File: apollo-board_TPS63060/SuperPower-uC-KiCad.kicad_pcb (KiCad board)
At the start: 4 copper layers, 45.1 x 45.1 mm, 114 parts, among them J1 JST_PH_S2B_thru, J10 Conn_01x13_Male, J11 Conn_01x04_Male, J3 Conn_01x02_Male, J4 DNP/JST_ZH_S2B_thru, J5 DNP/JST_XH_S2B_thru, J6 Conn_01x02_Male, Q1 DMN2019UTS, Q10 2N7002A, Q11 2N7002A, Q12 DMP2035UVT, Q13 DMP2035UVT, Q14 DMP2035UVT, Q15 DMN3023L, Q2 Si3421DV, Q3 DMN3023L, Q4 2N7002A, Q5 DMP2035UVT, Q6 BSS84-7-F, Q9 2N7002A, SW1 DNP/SKRKAEE020, U1 AP9101CK6-AYTRG1, U10 TPS63060, U2 USB-C, U3 IP4220CZ6, U4 LTC4162EUFD-LAD, U5 RV-3028-C7, U6 TPS70933DBV, U9 TPS63060

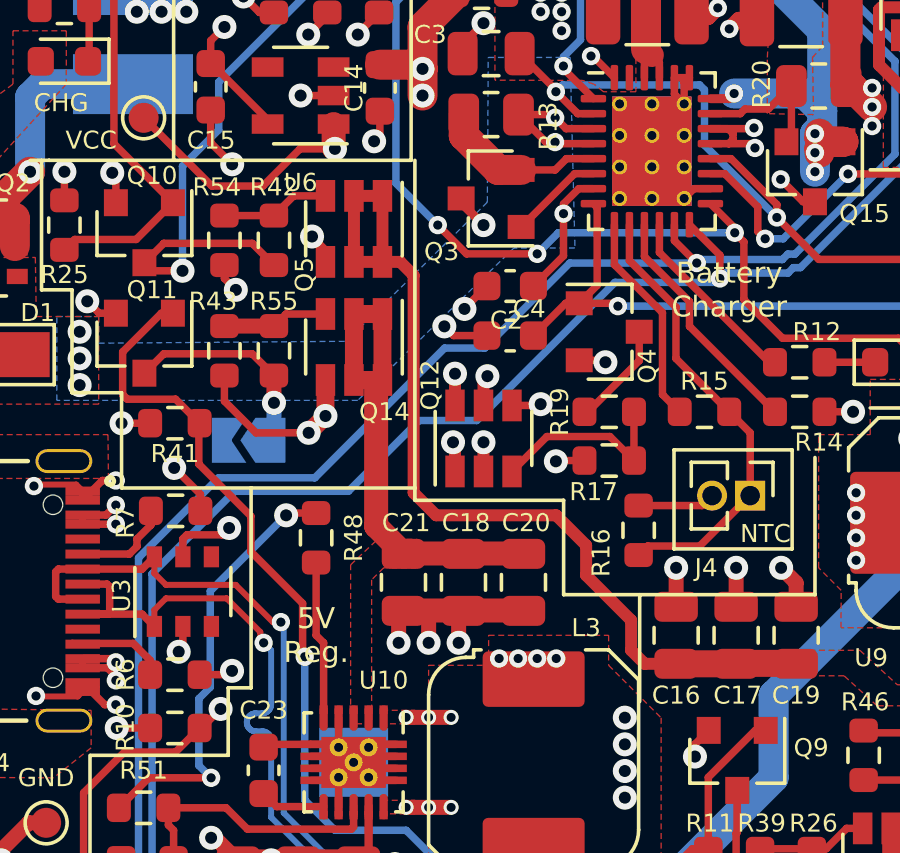
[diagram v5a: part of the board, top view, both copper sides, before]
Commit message: Improve Power Tracks width and Vias on Top Layer (+3.3V)
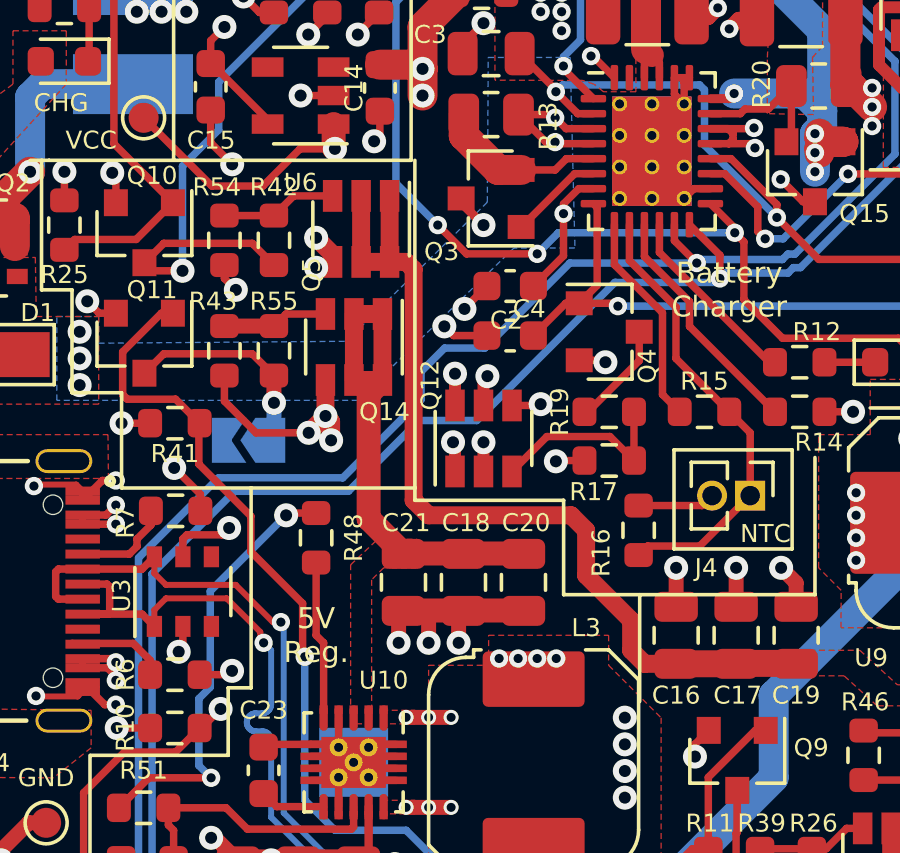
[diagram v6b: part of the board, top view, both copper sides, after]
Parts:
- moved Q5 0.24 mm to (133.6, 93.2)
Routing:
- net VCC: track 26.2 -> 27.7 mm, vias 11 -> 13
- net /Regulator and Cut-Off Module/3v3_Reg_Vin: track 31.1 -> 30.4 mm
- net /SCL: track 73.0 -> 73.6 mm
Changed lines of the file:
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@@
     (thickness 1.6)
     (drawings 122)
-    (tracks 1001)
+    (tracks 1009)
     (zones 0)
     (modules 114)
@@
   (layers
     (0 F.Cu signal)
-    (1 In1.Cu power hide)
-    (2 In2.Cu signal hide)
+    (1 In1.Cu power)
+    (2 In2.Cu signal)
     (31 B.Cu signal)
     (32 B.Adhes user)
@@
     (34 B.Paste user)
     (35 F.Paste user)
-    (36 B.SilkS user)
-    (37 F.SilkS user)
+    (36 B.SilkS user hide)
+    (37 F.SilkS user hide)
     (38 B.Mask user)
     (39 F.Mask user)
@@
   )
   (setup
-    (last_trace_width 0.25)
+    (last_trace_width 0.6)
     (user_trace_width 0.2)
     (user_trace_width 0.25)
@@
   )
   (module Package_TO_SOT_SMD:SOT-23-6 (layer F.Cu)
-    (at 133.35 93.218 270)
+    (at 133.589 93.218 270)
     (descr "6-pin SOT-23 package")
     (tags SOT-23-6)
@@
   (gr_line (start 160.5534 75.1332) (end 120.4722 75.1332) (layer Edge.Cuts) (width 0.05))
   (gr_line (start 120.523 120.2436) (end 160.5026 120.2436) (layer Edge.Cuts) (width 0.05))
+  (via (at 132.089 94.515) (size 0.8) (drill 0.4) (layers F.Cu B.Cu) (net 9))
   (via (at 153.035 80.9625) (size 0.8) (drill 0.4) (layers F.Cu B.Cu) (net 1))
   (segment (start 152.7885 81.209) (end 153.035 80.9625) (width 0.4) (layer F.Cu) (net 1))
@@
   (via (at 136.652 100.33) (size 0.8) (drill 0.4) (layers F.Cu B.Cu) (net 9))
   (via (at 137.668 100.33) (size 0.8) (drill 0.4) (layers F.Cu B.Cu) (net 9))
-  (via (at 131.953 93.472) (size 0.8) (drill 0.4) (layers F.Cu B.Cu) (net 9))
-  (segment (start 132.4 93.919) (end 131.953 93.472) (width 0.25) (layer F.Cu) (net 9))
-  (segment (start 132.4 94.318) (end 132.4 93.919) (width 0.25) (layer F.Cu) (net 9))
+  (via (at 132.089 93.515) (size 0.8) (drill 0.4) (layers F.Cu B.Cu) (net 9))
   (via (at 129.413 95.25) (size 0.8) (drill 0.4) (layers F.Cu B.Cu) (net 9))
   (segment (start 129.032 94.869) (end 129.413 95.25) (width 0.25) (layer F.Cu) (net 9))
@@
   (segment (start 129.032 98.107) (end 129.032 98.958) (width 0.25) (layer F.Cu) (net 9))
   (segment (start 129.032 98.958) (end 130.089 100.015) (width 0.25) (layer F.Cu) (net 9))
+  (segment (start 132.639 94.065) (end 132.089 93.515) (width 0.6) (layer F.Cu) (net 9))
+  (segment (start 132.639 94.318) (end 132.639 94.065) (width 0.6) (layer F.Cu) (net 9))
+  (segment (start 132.442 94.515) (end 132.639 94.318) (width 0.6) (layer F.Cu) (net 9))
+  (segment (start 132.089 94.515) (end 132.442 94.515) (width 0.6) (layer F.Cu) (net 9))
+  (via (at 132.589 100.265) (size 0.8) (drill 0.4) (layers F.Cu B.Cu) (net 9))
+  (segment (start 132.589 99.643) (end 132.4 99.454) (width 0.6) (layer F.Cu) (net 9))
+  (segment (start 132.589 100.265) (end 132.589 99.643) (width 0.6) (layer F.Cu) (net 9))
   (segment (start 127.6477 104.1484) (end 127.6477 103.5484) (width 0.25) (layer F.Cu) (net 12))
   (segment (start 128.960468 103.41601) (end 129.188978 103.1875) (width 0.25) (layer F.Cu) (net 12))
@@
   (segment (start 140.543888 94.355477) (end 144.776433 94.355477) (width 0.25) (layer B.Cu) (net 14))
   (segment (start 137.707368 97.191997) (end 140.543888 94.355477) (width 0.25) (layer B.Cu) (net 14))
-  (segment (start 132.047001 101.515) (end 136.370004 97.191997) (width 0.25) (layer B.Cu) (net 14))
-  (segment (start 128.839 101.515) (end 132.047001 101.515) (width 0.25) (layer B.Cu) (net 14))
-  (segment (start 126.168989 104.185011) (end 128.839 101.515) (width 0.25) (layer B.Cu) (net 14))
   (segment (start 136.370004 97.191997) (end 137.707368 97.191997) (width 0.25) (layer B.Cu) (net 14))
+  (segment (start 135.589 98.903364) (end 135.589 97.973001) (width 0.25) (layer B.Cu) (net 14))
+  (segment (start 132.977364 101.515) (end 135.589 98.903364) (width 0.25) (layer B.Cu) (net 14))
+  (segment (start 135.589 97.973001) (end 136.370004 97.191997) (width 0.25) (layer B.Cu) (net 14))
+  (segment (start 128.839 101.515) (end 132.977364 101.515) (width 0.25) (layer B.Cu) (net 14))
+  (segment (start 126.168989 104.185011) (end 128.839 101.515) (width 0.25) (layer B.Cu) (net 14))
+  (segment (start 125.089 118.739) (end 125.089 115.39) (width 0.25) (layer B.Cu) (net 14))
   (segment (start 126.168989 114.310011) (end 126.168989 104.185011) (width 0.25) (layer B.Cu) (net 14))
   (segment (start 125.089 115.39) (end 126.168989 114.310011) (width 0.25) (layer B.Cu) (net 14))
-  (segment (start 125.089 118.739) (end 125.089 115.39) (width 0.25) (layer B.Cu) (net 14))
   (segment (start 125.222 118.872) (end 125.089 118.739) (width 0.25) (layer B.Cu) (net 14))
   (segment (start 130.683 100.465) (end 130.564 100.584) (width 0.6) (layer B.Cu) (net 31))
@@
   (segment (start 158.089 89.515) (end 161.29 89.535) (width 0.5) (layer F.Cu) (net 63))
   (segment (start 158.339 89.515) (end 158.089 89.515) (width 0.5) (layer F.Cu) (net 63))
-  (segment (start 134.3 92.118) (end 133.35 92.118) (width 0.4) (layer F.Cu) (net 64))
-  (segment (start 134.3 94.318) (end 133.35 94.318) (width 0.4) (layer F.Cu) (net 64))
-  (segment (start 133.35 92.118) (end 133.35 94.318) (width 0.4) (layer F.Cu) (net 64))
-  (segment (start 134.3 94.318) (end 134.3 92.118) (width 0.4) (layer F.Cu) (net 64))
   (segment (start 146.074 107.715) (end 146.089 107.7) (width 0.5) (layer F.Cu) (net 64))
   (segment (start 144.089 107.715) (end 146.074 107.715) (width 0.9) (layer F.Cu) (net 64))
   (segment (start 146.089 107.7) (end 148.089 107.7) (width 0.9) (layer F.Cu) (net 64))
-  (segment (start 142.589 106.265) (end 142.589 107.265) (width 0.4) (layer F.Cu) (net 64))
-  (segment (start 140.089 102.765) (end 141.089 103.765) (width 0.4) (layer F.Cu) (net 64))
-  (segment (start 136.089 102.765) (end 140.089 102.765) (width 0.4) (layer F.Cu) (net 64))
-  (segment (start 141.089 103.765) (end 141.089 104.765) (width 0.4) (layer F.Cu) (net 64))
-  (segment (start 135.339 102.015) (end 136.089 102.765) (width 0.4) (layer F.Cu) (net 64))
-  (segment (start 141.089 104.765) (end 142.589 106.265) (width 0.4) (layer F.Cu) (net 64))
-  (segment (start 135.339 94.765) (end 135.339 102.015) (width 0.4) (layer F.Cu) (net 64))
-  (segment (start 143.039 107.715) (end 144.089 107.715) (width 0.4) (layer F.Cu) (net 64))
-  (segment (start 142.589 107.265) (end 143.039 107.715) (width 0.4) (layer F.Cu) (net 64))
-  (segment (start 134.892 94.318) (end 135.339 94.765) (width 0.4) (layer F.Cu) (net 64))
-  (segment (start 134.3 94.318) (end 134.892 94.318) (width 0.4) (layer F.Cu) (net 64))
+  (segment (start 133.589 92.118) (end 133.589 94.318) (width 0.6) (layer F.Cu) (net 64))
+  (segment (start 134.539 94.318) (end 133.589 94.318) (width 0.6) (layer F.Cu) (net 64))
+  (segment (start 134.539 92.118) (end 134.539 94.318) (width 0.6) (layer F.Cu) (net 64))
+  (segment (start 143.039 107.715) (end 144.089 107.715) (width 0.6) (layer F.Cu) (net 64))
+  (segment (start 142.589 107.265) (end 143.039 107.715) (width 0.6) (layer F.Cu) (net 64))
+  (segment (start 141.089 104.765) (end 142.589 106.265) (width 0.6) (layer F.Cu) (net 64))
+  (segment (start 141.089 103.265) (end 141.089 104.765) (width 0.6) (layer F.Cu) (net 64))
+  (segment (start 142.589 106.265) (end 142.589 107.265) (width 0.6) (layer F.Cu) (net 64))
+  (segment (start 135.839 102.765) (end 140.589 102.765) (width 0.6) (layer F.Cu) (net 64))
+  (segment (start 135.339 102.265) (end 135.839 102.765) (width 0.6) (layer F.Cu) (net 64))
+  (segment (start 135.339 94.568) (end 135.339 102.265) (width 0.6) (layer F.Cu) (net 64))
+  (segment (start 140.589 102.765) (end 141.089 103.265) (width 0.6) (layer F.Cu) (net 64))
+  (segment (start 135.089 94.318) (end 135.339 94.568) (width 0.6) (layer F.Cu) (net 64))
+  (segment (start 134.539 94.318) (end 135.089 94.318) (width 0.6) (layer F.Cu) (net 64))
   (segment (start 155.064 111.661) (end 154 112.725) (width 0.25) (layer F.Cu) (net 65))
   (segment (start 155.064 110.015) (end 155.064 111.661) (width 0.25) (layer F.Cu) (net 65))
@@
   (segment (start 134.3 96.055) (end 134.3 98.255) (width 0.6) (layer F.Cu) (net 67))
   (segment (start 134.089 98.466) (end 134.3 98.255) (width 0.6) (layer F.Cu) (net 67))
-  (segment (start 134.089 103.1274) (end 134.089 98.466) (width 0.8) (layer F.Cu) (net 67))
-  (segment (start 135 104.0384) (end 134.089 103.1274) (width 0.8) (layer F.Cu) (net 67))
   (segment (start 139 104.0384) (end 135 104.0384) (width 0.8) (layer F.Cu) (net 67))
+  (segment (start 135 104.0384) (end 133.839 102.8774) (width 0.8) (layer F.Cu) (net 67))
+  (segment (start 133.839 102.8774) (end 133.839 98.716) (width 0.8) (layer F.Cu) (net 67))
+  (segment (start 133.839 98.716) (end 134.089 98.466) (width 0.8) (layer F.Cu) (net 67))
   (segment (start 130.774 112.475) (end 130.339 112.04) (width 0.25) (layer F.Cu) (net 68))
   (segment (start 132.339 112.475) (end 130.774 112.475) (width 0.25) (layer F.Cu) (net 68))

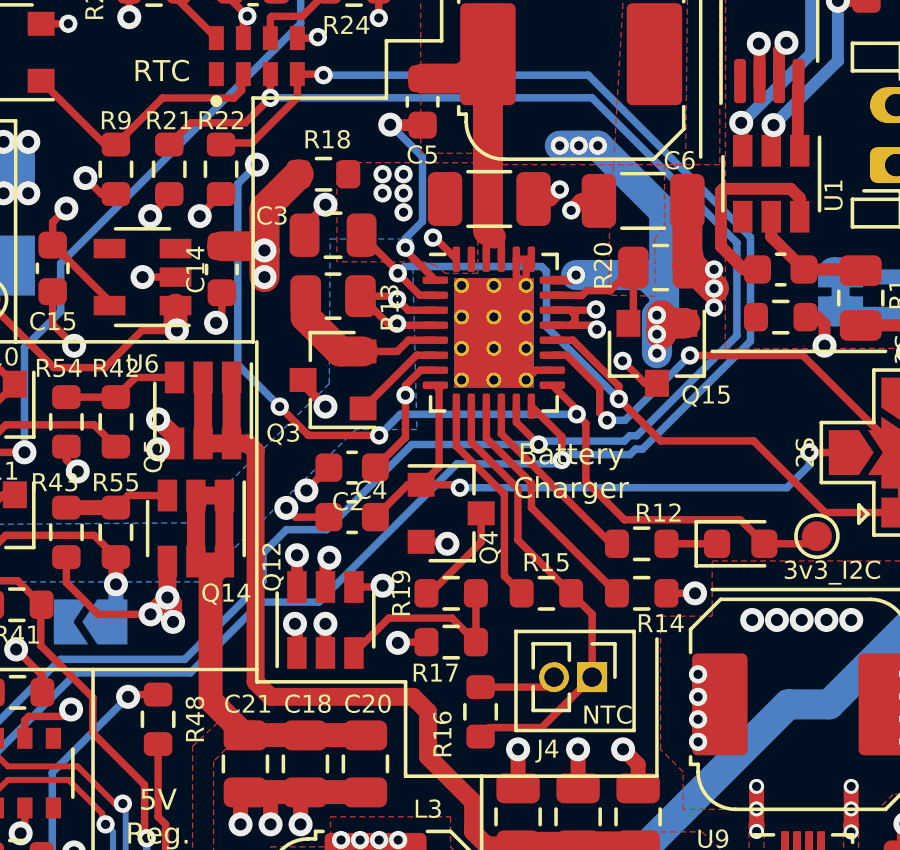
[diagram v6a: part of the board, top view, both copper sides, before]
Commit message: Improve Tracks width and vias around LTC4162-L
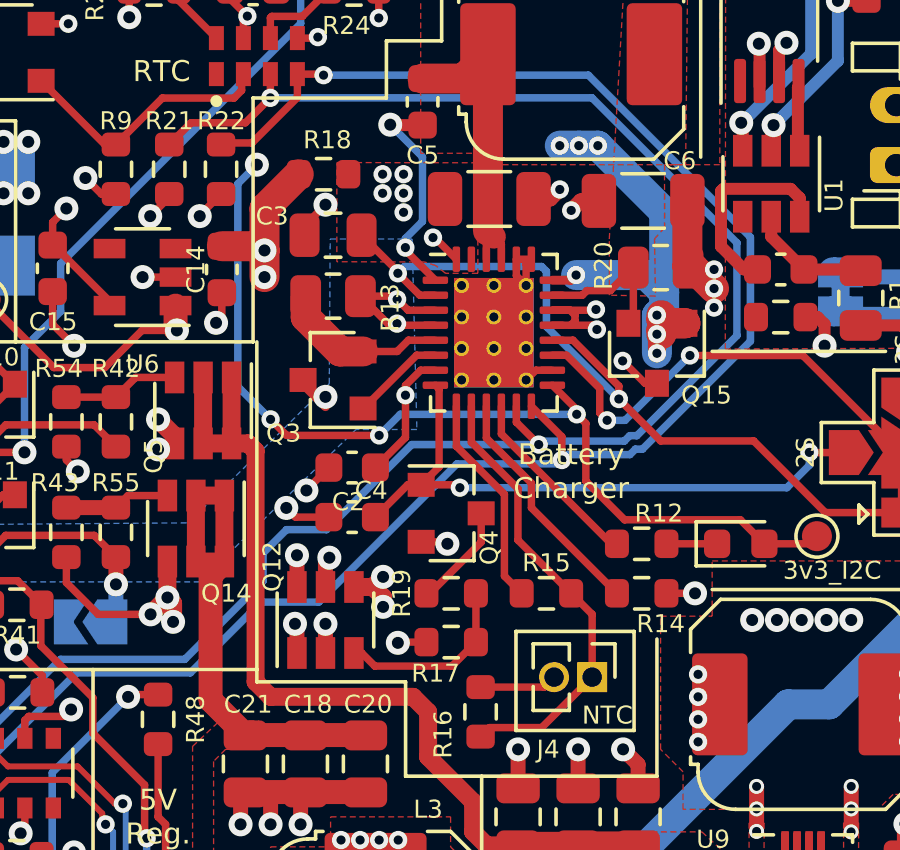
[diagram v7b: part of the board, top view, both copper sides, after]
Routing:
- net VCCQ: track 10.1 -> 11.0 mm, vias 11 -> 12
- net Net-(Q15-Pad1): track 15.3 -> 16.0 mm

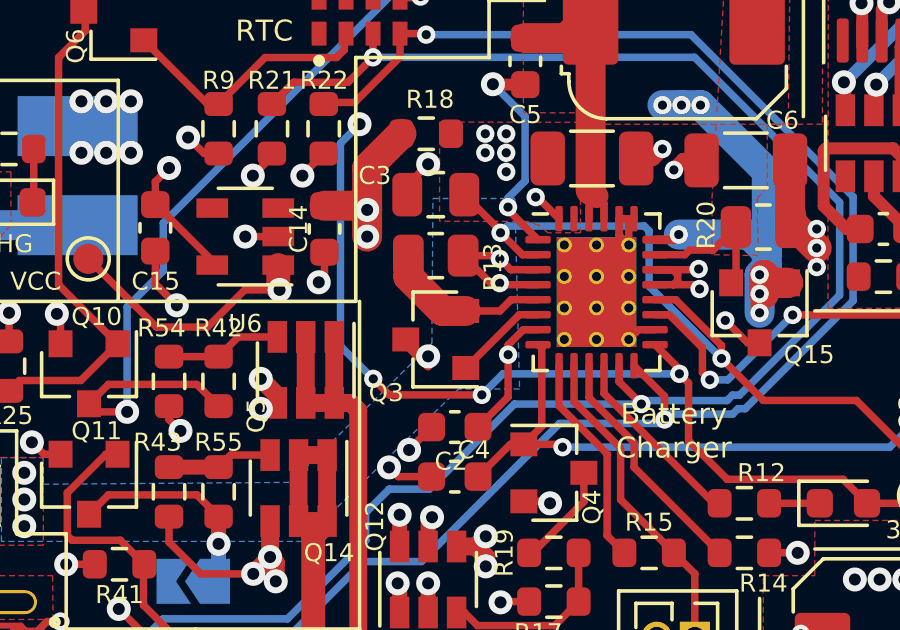
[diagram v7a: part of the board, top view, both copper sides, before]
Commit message: Improve Tracks width and Vias around LTC4162-L (Q3)
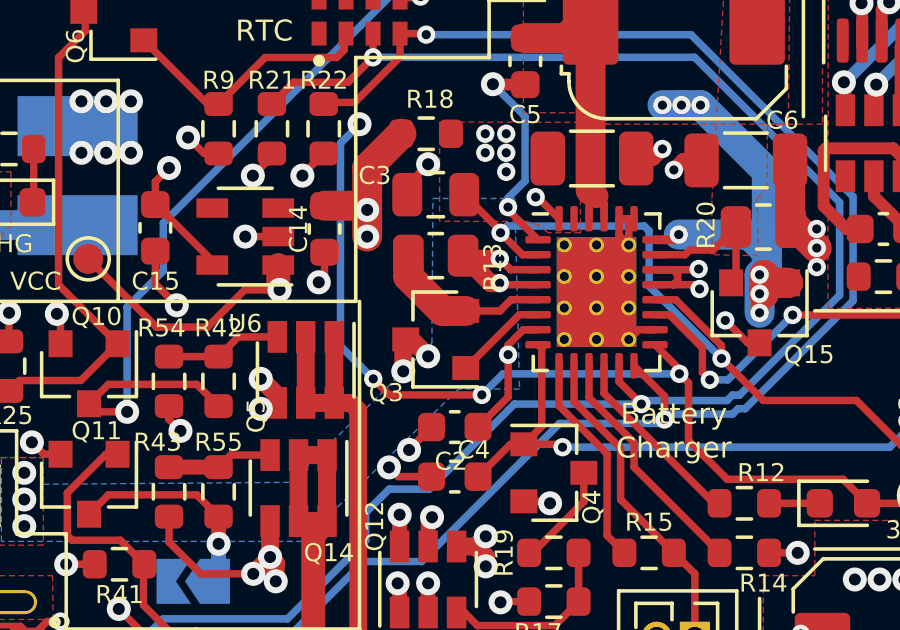
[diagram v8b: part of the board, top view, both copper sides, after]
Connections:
- net Net-(Q3-Pad1) renamed /Charging Module/INFET
- net Net-(Q3-Pad2) renamed /Charging Module/CLP
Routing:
- net VDD: track 5.74 -> 6.76 mm, vias 5 -> 6
